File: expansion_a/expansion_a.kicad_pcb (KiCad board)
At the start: 4 copper layers, 58.7 x 55.2 mm, 50 parts, among them J101 Conn_01x08, J1101 Conn_01x03, J1102 Conn_01x06, J201 Conn_01x03, J202 Conn_01x06, U1001 GAQY212G1S, U101 74HC373, U102 74HC595, U301 GAQY212G1S, U401 GAQY212G1S, U501 GAQY212G1S, U601 GAQY212G1S, U701 GAQY212G1S, U801 GAQY212G1S, U901 GAQY212G1S

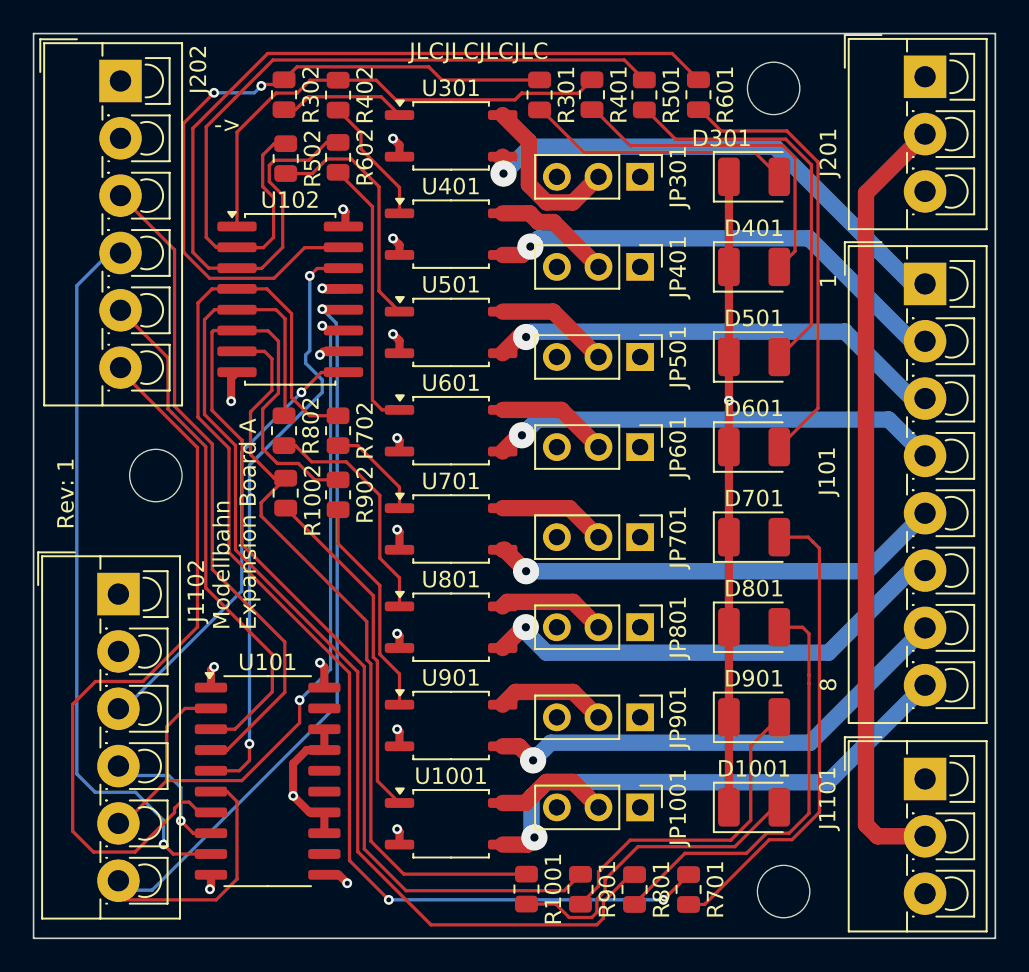
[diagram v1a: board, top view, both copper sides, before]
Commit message: Add capacitors for ic
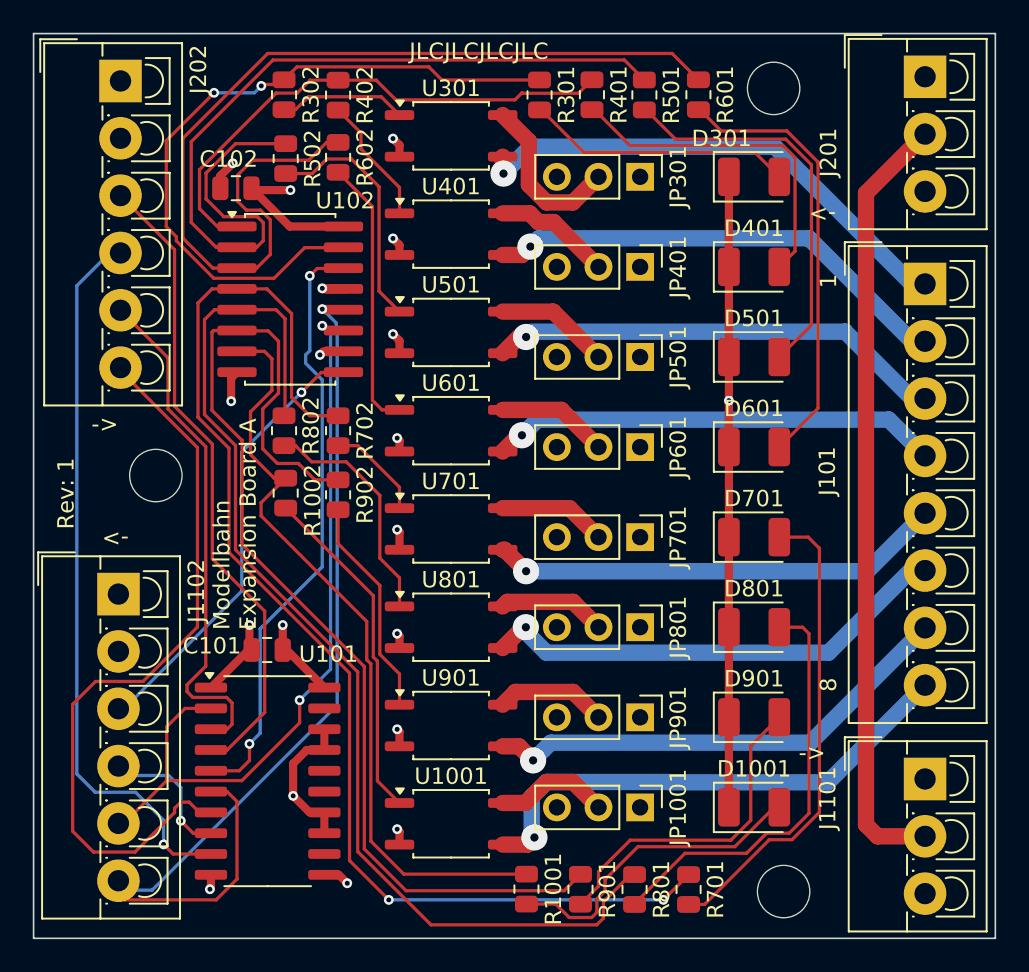
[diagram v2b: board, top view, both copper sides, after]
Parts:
- added C101: 100n, Capacitor_SMD:C_0805_2012Metric, F.Cu at (82.9, 71.6)
- added C102: 100n, Capacitor_SMD:C_0805_2012Metric, F.Cu at (81.0, 43.4)
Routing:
- net VCC: track 4.37 -> 15.3 mm
- net GND: track 84.9 -> 90.2 mm, vias 15 -> 16
- net /set3: track 48.6 -> 52.7 mm
- net /set2: track 29.8 -> 32.4 mm
- net /Connector out/CLK: track 47.3 -> 46.2 mm
- net /set4: track 58.9 -> 60.0 mm
- net /Connector in/MOSI: track 40.4 -> 39.4 mm
- net /set1: track 42.9 -> 43.6 mm
